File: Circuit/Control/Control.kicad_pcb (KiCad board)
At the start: 2 copper layers, 57.1 x 34.3 mm, 38 parts, among them J1 +S G -S, J2 NO G NC, J3 Power, J4 Bypass SW, J5 Force on SW, Q1 2N2222, Q2 2N2222, U1 LM393, U2 NE555

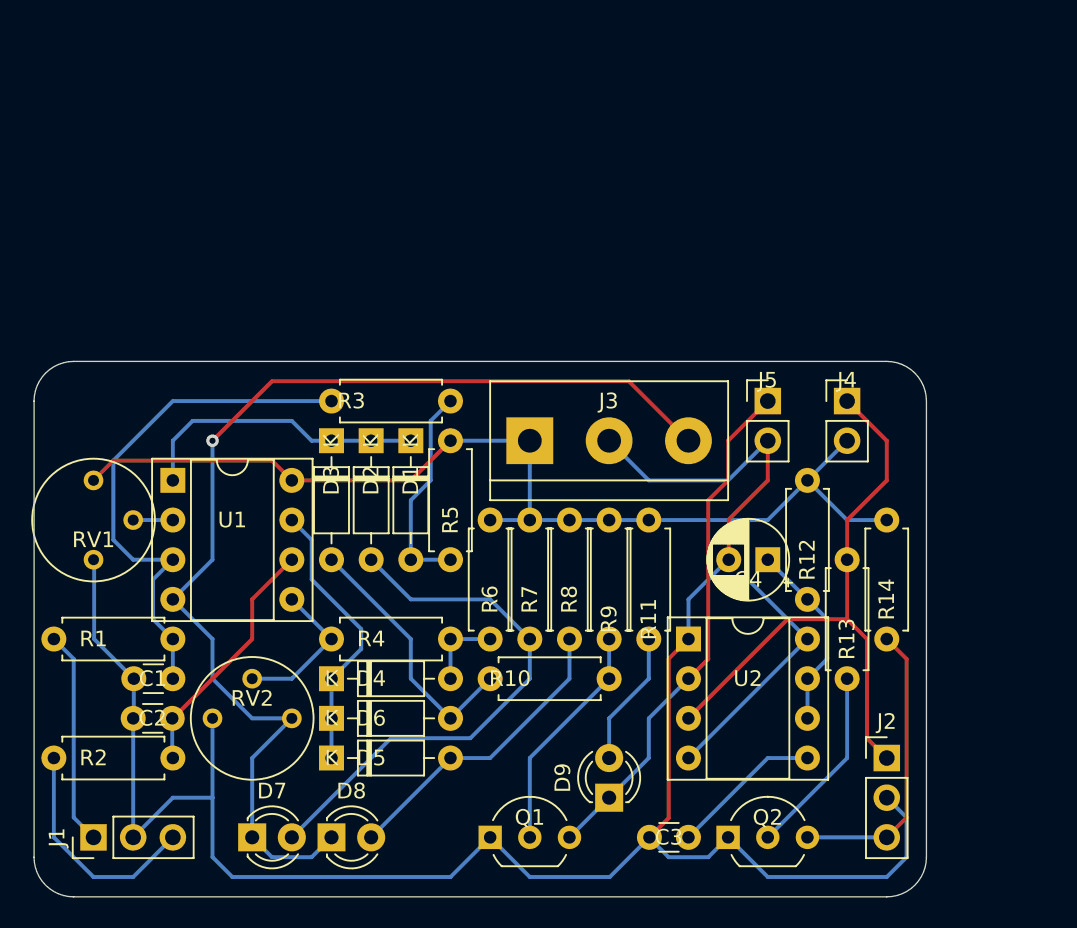
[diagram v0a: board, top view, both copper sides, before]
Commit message: [Circuit] Use a single 12V power for control module
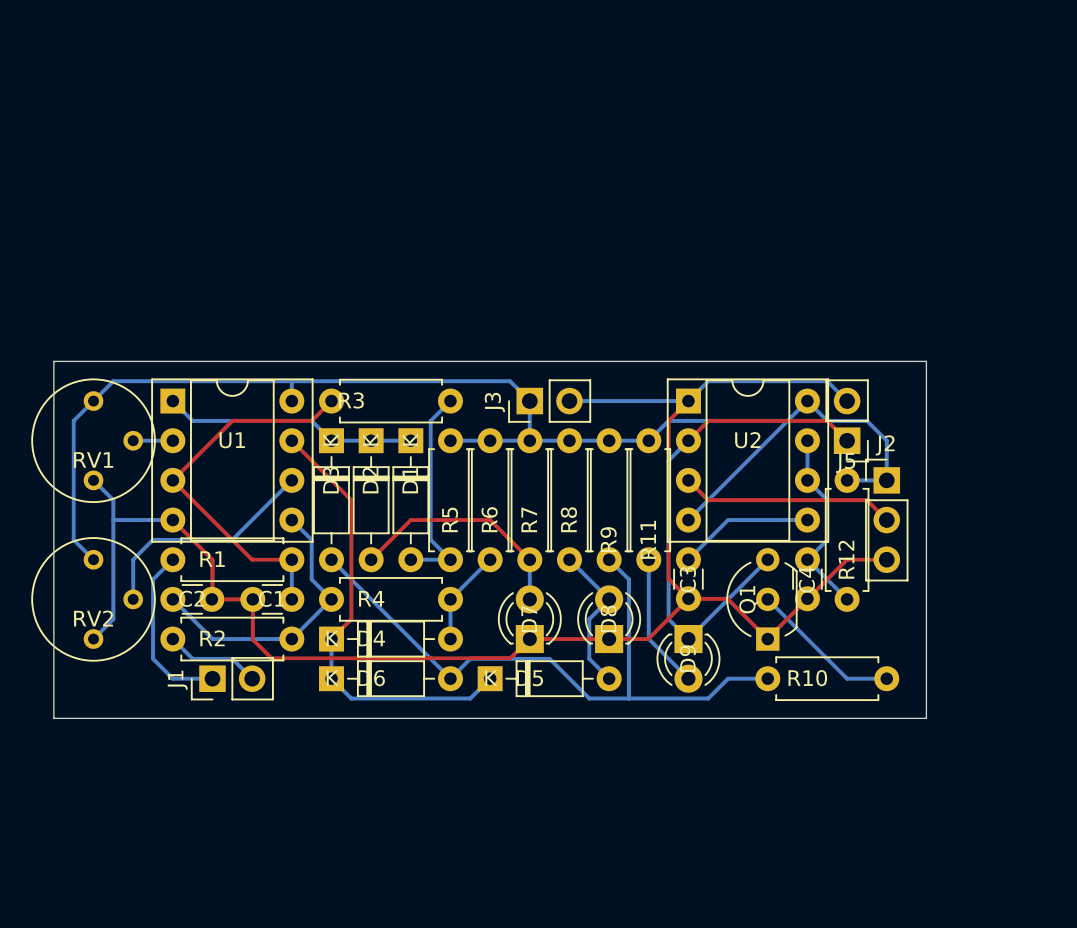
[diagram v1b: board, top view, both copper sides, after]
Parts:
- removed J4: Bypass SW, Connector_PinHeader_2.54mm:PinHeader_1x02_P2.54mm_Vertical
- removed Q2: 2N2222, Package_TO_SOT_THT:TO-92_Inline_Wide
- removed R13: 2K, Resistor_THT:R_Axial_DIN0207_L6.3mm_D2.5mm_P7.62mm_Horizontal
- removed R14: 1K, Resistor_THT:R_Axial_DIN0207_L6.3mm_D2.5mm_P7.62mm_Horizontal
- C4: value 1uF -> 0.1uF; footprint Capacitor_THT:CP_Radial_D5.0mm_P2.50mm -> Capacitor_THT:C_Disc_D3.0mm_W1.6mm_P2.50mm
- J1: value +S G -S -> Signal; footprint Connector_PinHeader_2.54mm:PinHeader_1x03_P2.54mm_Vertical -> Connector_PinHeader_2.54mm:PinHeader_1x02_P2.54mm_Vertical
- J2: value NO G NC -> 12V NO G
- J3: footprint TerminalBlock:TerminalBlock_bornier-3_P5.08mm -> Connector_PinHeader_2.54mm:PinHeader_1x02_P2.54mm_Vertical
- R10, R9: value 100K -> 3K3
- R11: value 1K -> 2K
- R12: value 20K -> 220K
- R3: value 100K -> 220K
- R4: value 1M -> 220K
- moved D7 21.8 mm to (149.9, 83.8), turned to 90 degrees
- moved D8 21.8 mm to (154.9, 83.8), turned to 90 degrees
- moved Q1 21.8 mm to (165.1, 83.8), turned to 90 degrees
- moved C3 17.8 mm to (160.0, 78.7), turned to 270 degrees
- moved J2 17.8 mm to (172.7, 73.7)
- moved U2 15.2 mm to (160.0, 68.6)
- moved RV2 12.7 mm to (121.9, 78.7), turned to 180 degrees
- moved J1 12.7 mm to (129.5, 86.4)
- moved D9 11.4 mm to (160.0, 83.8), turned to 270 degrees
- moved D5 11.4 mm to (147.3, 86.4)
- moved R2 10.8 mm to (134.6, 83.8)
- moved R10 10.2 mm to (165.1, 86.4), turned to 0 degrees
- moved C1 9.16 mm to (134.6, 81.3)
- moved R1 9.16 mm to (134.6, 78.7)
- moved C2 8.03 mm to (127.0, 81.3)
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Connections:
- net Net-(J1-Pad1) renamed /CapacitorSignal1
- C2 pad 1: GND -> Net-(C2-Pad1)
- C2 pad 2: Net-(C2-Pad2) -> GND
- D7 pad 1: -12V -> GND
- D8 pad 1: -12V -> GND
- J1 pad 2: GND -> /CapacitorSignal2
- J2 pad 1: Net-(J2-Pad1) -> +12V
- J2 pad 2: GND -> /ControlSignal
- J2 pad 3: Net-(J2-Pad3) -> GND
- R10 pad 1: Net-(Q1-Pad2) -> Net-(D3-Pad2)
- R10 pad 2: Net-(D3-Pad2) -> Net-(Q1-Pad2)
- R2 pad 1: Net-(C2-Pad2) -> Net-(C2-Pad1)
- R2 pad 2: Net-(J1-Pad3) -> /CapacitorSignal2
- R4 pad 1: Net-(R4-Pad1) -> Net-(C2-Pad1)
- R9 pad 2: Net-(Q1-Pad2) -> Net-(D3-Pad2)
- RV2 pad 1: GND -> +12V
- RV2 pad 2: Net-(R4-Pad1) -> Net-(RV2-Pad2)
- RV2 pad 3: -12V -> GND
- U1 pad 4: -12V -> GND
- U1 pad 5: Net-(R4-Pad1) -> Net-(C2-Pad1)
- U1 pad 6: Net-(C2-Pad2) -> Net-(RV2-Pad2)
- U2 pad 3: Net-(J2-Pad1) -> /ControlSignal
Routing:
- net -12V: track 71.9 -> 0.00 mm, vias 1 -> 0
- net Net-(J2-Pad1): track 38.8 -> 0.00 mm
- net Net-(D3-Pad2): track 16.9 -> 42.6 mm
- net GND: track 129.9 -> 104.9 mm
- net Net-(D2-Pad2): track 34.3 -> 14.8 mm
- net Net-(J2-Pad3): track 18.8 -> 0.00 mm
- net Net-(C2-Pad1): track 0.00 -> 18.5 mm
- net Net-(C2-Pad2): track 16.0 -> 0.00 mm
- net Net-(RV2-Pad2): track 0.00 -> 14.8 mm
- net Net-(J1-Pad3): track 14.8 -> 0.00 mm
- net /ControlSignal: track 0.00 -> 13.8 mm
- net Net-(Q2-Pad2): track 12.3 -> 0.00 mm
- net Net-(D4-Pad1): track 17.9 -> 28.6 mm
- net Net-(D5-Pad2): track 19.4 -> 9.72 mm
- net Net-(R4-Pad1): track 9.72 -> 0.00 mm
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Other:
- board size 57.1 x 34.3 mm -> 55.9 x 22.9 mm
- board text added: "M. Gong"

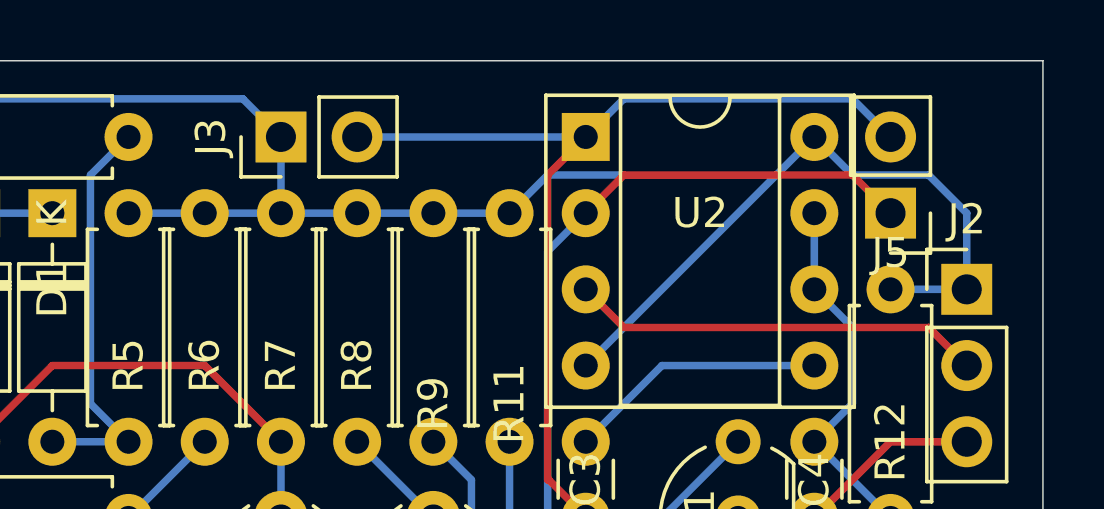
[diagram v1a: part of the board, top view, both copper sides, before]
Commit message: [Circuit] Add a separated battery for Control module
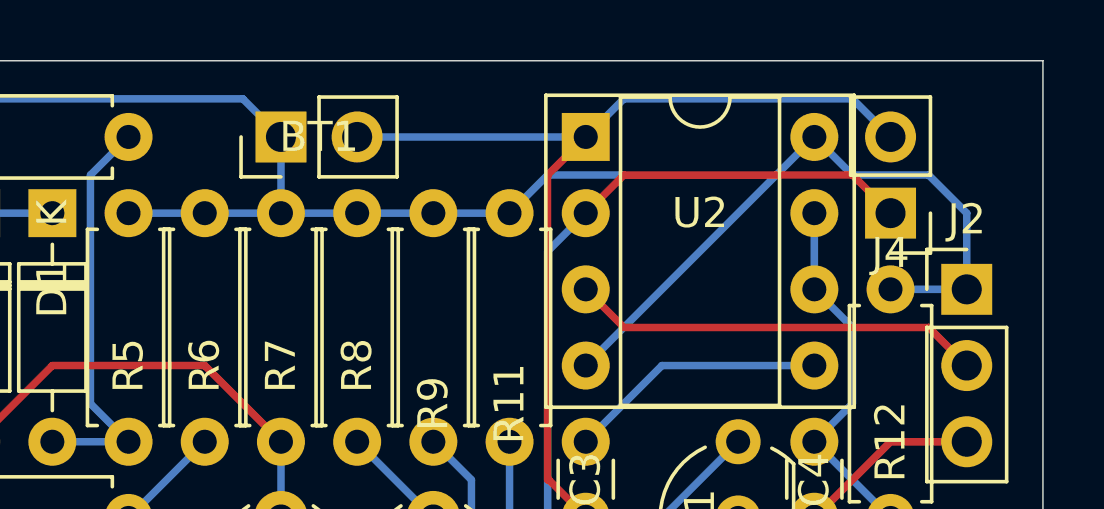
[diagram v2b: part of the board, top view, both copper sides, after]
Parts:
- removed J3: Power, Connector_PinHeader_2.54mm:PinHeader_1x02_P2.54mm_Vertical
- added BT1: 12V Battery, Connector_PinHeader_2.54mm:PinHeader_1x02_P2.54mm_Vertical, F.Cu at (149.9, 68.6)
- renumbered J5 to J4
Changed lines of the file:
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@@
+  )
+  (module Connector_PinHeader_2.54mm:PinHeader_1x02_P2.54mm_Vertical (layer F.Cu)
+    (at 149.86 68.58 90)
+    (descr "Through hole straight pin header, 1x02, 2.54mm pitch, single row")
+    (tags "Through hole pin header THT 1x02 2.54mm single row")
+    (fp_text reference BT1 (at 0 1.27 180) (layer F.SilkS)
+      (effects (font (size 1 1) (thickness 0.15)))
+    )
+    (fp_text value "12V Battery" (at 1.27 1.27 180) (layer F.Fab)
+      (effects (font (size 1 1) (thickness 0.15)))
+    )
+    (fp_text user %R (at 0 1.27) (layer F.Fab)
+      (effects (font (size 1 1) (thickness 0.15)))
+    )
+    (fp_line (start 1.8 -1.8) (end -1.8 -1.8) (layer F.CrtYd) (width 0.05))
+    (fp_line (start 1.8 4.35) (end 1.8 -1.8) (layer F.CrtYd) (width 0.05))
+    (fp_line (start -1.8 4.35) (end 1.8 4.35) (layer F.CrtYd) (width 0.05))
+    (fp_line (start -1.8 -1.8) (end -1.8 4.35) (layer F.CrtYd) (width 0.05))
+    (fp_line (start -1.33 -1.33) (end 0 -1.33) (layer F.SilkS) (width 0.12))
+    (fp_line (start -1.33 0) (end -1.33 -1.33) (layer F.SilkS) (width 0.12))
+    (fp_line (start -1.33 1.27) (end 1.33 1.27) (layer F.SilkS) (width 0.12))
+    (fp_line (start 1.33 1.27) (end 1.33 3.87) (layer F.SilkS) (width 0.12))
+    (fp_line (start -1.33 1.27) (end -1.33 3.87) (layer F.SilkS) (width 0.12))
+    (fp_line (start -1.33 3.87) (end 1.33 3.87) (layer F.SilkS) (width 0.12))
+    (fp_line (start -1.27 -0.635) (end -0.635 -1.27) (layer F.Fab) (width 0.1))
+    (fp_line (start -1.27 3.81) (end -1.27 -0.635) (layer F.Fab) (width 0.1))
+    (fp_line (start 1.27 3.81) (end -1.27 3.81) (layer F.Fab) (width 0.1))
+    (fp_line (start 1.27 -1.27) (end 1.27 3.81) (layer F.Fab) (width 0.1))
+    (fp_line (start -0.635 -1.27) (end 1.27 -1.27) (layer F.Fab) (width 0.1))
+    (pad 2 thru_hole oval (at 0 2.54 90) (size 1.7 1.7) (drill 1) (layers *.Cu *.Mask)
+      (net 2 GND))
+    (pad 1 thru_hole rect (at 0 0 90) (size 1.7 1.7) (drill 1) (layers *.Cu *.Mask)
+      (net 11 +12V))
+    (model ${KISYS3DMOD}/Connector_PinHeader_2.54mm.3dshapes/PinHeader_1x02_P2.54mm_Vertical.wrl
+      (at (xyz 0 0 0))
+      (scale (xyz 1 1 1))
+      (rotate (xyz 0 0 0))
+    )
   )
   (module Connector_PinHeader_2.54mm:PinHeader_1x02_P2.54mm_Vertical (layer F.Cu)
@@
       (net 4 "Net-(C4-Pad1)"))
     (model ${KISYS3DMOD}/Capacitor_THT.3dshapes/C_Disc_D3.0mm_W1.6mm_P2.50mm.wrl
-      (at (xyz 0 0 0))
-      (scale (xyz 1 1 1))
-      (rotate (xyz 0 0 0))
-    )
-  )
-  (module Connector_PinHeader_2.54mm:PinHeader_1x02_P2.54mm_Vertical (layer F.Cu)
-    (at 149.86 68.58 90)
-    (descr "Through hole straight pin header, 1x02, 2.54mm pitch, single row")
-    (tags "Through hole pin header THT 1x02 2.54mm single row")
-    (fp_text reference J3 (at 0 -2.33 90) (layer F.SilkS)
-      (effects (font (size 1 1) (thickness 0.15)))
-    )
-    (fp_text value Power (at 1.27 1.27 180) (layer F.Fab)
-      (effects (font (size 1 1) (thickness 0.15)))
-    )
-    (fp_line (start -0.635 -1.27) (end 1.27 -1.27) (layer F.Fab) (width 0.1))
-    (fp_line (start 1.27 -1.27) (end 1.27 3.81) (layer F.Fab) (width 0.1))
-    (fp_line (start 1.27 3.81) (end -1.27 3.81) (layer F.Fab) (width 0.1))
-    (fp_line (start -1.27 3.81) (end -1.27 -0.635) (layer F.Fab) (width 0.1))
-    (fp_line (start -1.27 -0.635) (end -0.635 -1.27) (layer F.Fab) (width 0.1))
-    (fp_line (start -1.33 3.87) (end 1.33 3.87) (layer F.SilkS) (width 0.12))
-    (fp_line (start -1.33 1.27) (end -1.33 3.87) (layer F.SilkS) (width 0.12))
-    (fp_line (start 1.33 1.27) (end 1.33 3.87) (layer F.SilkS) (width 0.12))
-    (fp_line (start -1.33 1.27) (end 1.33 1.27) (layer F.SilkS) (width 0.12))
-    (fp_line (start -1.33 0) (end -1.33 -1.33) (layer F.SilkS) (width 0.12))
-    (fp_line (start -1.33 -1.33) (end 0 -1.33) (layer F.SilkS) (width 0.12))
-    (fp_line (start -1.8 -1.8) (end -1.8 4.35) (layer F.CrtYd) (width 0.05))
-    (fp_line (start -1.8 4.35) (end 1.8 4.35) (layer F.CrtYd) (width 0.05))
-    (fp_line (start 1.8 4.35) (end 1.8 -1.8) (layer F.CrtYd) (width 0.05))
-    (fp_line (start 1.8 -1.8) (end -1.8 -1.8) (layer F.CrtYd) (width 0.05))
-    (fp_text user %R (at 0 1.27) (layer F.Fab)
-      (effects (font (size 1 1) (thickness 0.15)))
-    )
-    (pad 1 thru_hole rect (at 0 0 90) (size 1.7 1.7) (drill 1) (layers *.Cu *.Mask)
-      (net 11 +12V))
-    (pad 2 thru_hole oval (at 0 2.54 90) (size 1.7 1.7) (drill 1) (layers *.Cu *.Mask)
-      (net 2 GND))
-    (model ${KISYS3DMOD}/Connector_PinHeader_2.54mm.3dshapes/PinHeader_1x02_P2.54mm_Vertical.wrl
       (at (xyz 0 0 0))
       (scale (xyz 1 1 1))
@@
     (descr "Through hole straight pin header, 1x02, 2.54mm pitch, single row")
     (tags "Through hole pin header THT 1x02 2.54mm single row")
-    (fp_text reference J5 (at 0 -1.33) (layer F.SilkS)
-      (effects (font (size 1 1) (thickness 0.15)))
-    )
+    (fp_text reference J4 (at 0 -1.33) (layer F.SilkS)
+      (effects (font (size 1 1) (thickness 0.15)))
+    )

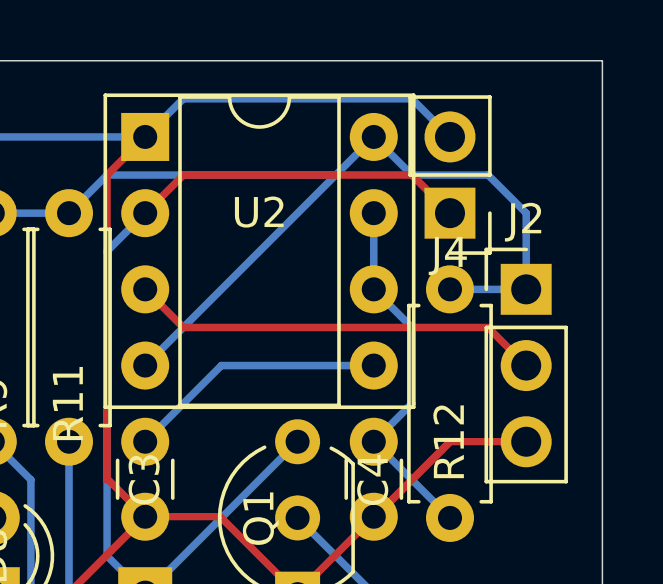
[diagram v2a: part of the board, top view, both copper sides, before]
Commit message: [Circuit] Merge capacitor bank, converter, and bleeder circuits into one
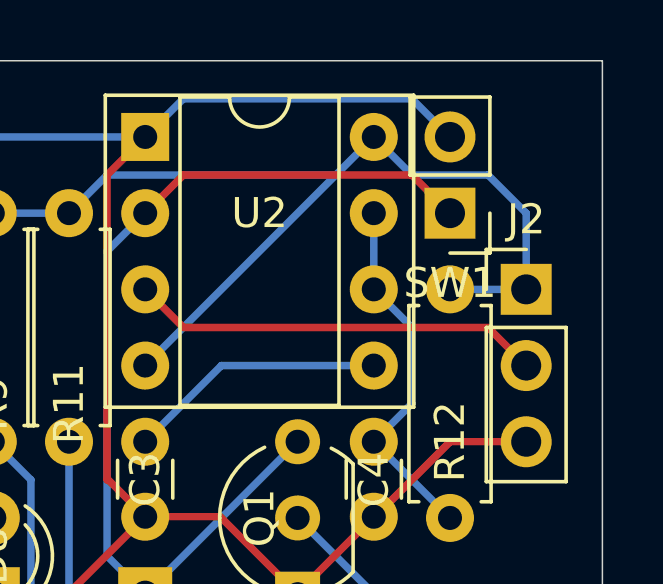
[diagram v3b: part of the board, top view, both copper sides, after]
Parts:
- removed J4: Force on SW, Connector_PinHeader_2.54mm:PinHeader_1x02_P2.54mm_Vertical
- added SW1: Force on, Connector_PinHeader_2.54mm:PinHeader_1x02_P2.54mm_Vertical, F.Cu at (170.2, 71.1)
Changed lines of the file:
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@@
     (descr "Through hole straight pin header, 1x02, 2.54mm pitch, single row")
     (tags "Through hole pin header THT 1x02 2.54mm single row")
-    (fp_text reference J4 (at 0 -1.33) (layer F.SilkS)
+    (fp_text reference SW1 (at 0 -2.33) (layer F.SilkS)
       (effects (font (size 1 1) (thickness 0.15)))
     )
-    (fp_text value "Force on SW" (at 0 0 90) (layer F.Fab)
+    (fp_text value "Force on" (at 0 3.81) (layer F.Fab)
       (effects (font (size 1 1) (thickness 0.15)))
     )
